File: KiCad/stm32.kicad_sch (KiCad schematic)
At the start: 20 parts, among them J15 Conn_01x04, J16 Conn_01x04, J17 Conn_01x04, J18 Conn_01x05, U7 STM32F030C8Tx, Y1 25MHz

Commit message: Add more footprints
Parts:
- C183, C184, C185, C186, C187, C188, C189, C190, C191, C192: footprint (none) -> Capacitor_SMD:C_0603_1608Metric
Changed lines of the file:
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@@
 			)
 		)
-		(property "Footprint" ""
+		(property "Footprint" "Capacitor_SMD:C_0603_1608Metric"
 			(at 110.49 80.01 0)
 			(effects
@@
 			)
 		)
-		(property "Footprint" ""
+		(property "Footprint" "Capacitor_SMD:C_0603_1608Metric"
 			(at 132.08 77.47 0)
 			(effects
@@
 			)
 		)
-		(property "Footprint" ""
+		(property "Footprint" "Capacitor_SMD:C_0603_1608Metric"
 			(at 110.49 74.93 0)
 			(effects
@@
 			)
 		)
-		(property "Footprint" ""
+		(property "Footprint" "Capacitor_SMD:C_0603_1608Metric"
 			(at 132.08 80.01 0)
 			(effects
@@
 			)
 		)
-		(property "Footprint" ""
+		(property "Footprint" "Capacitor_SMD:C_0603_1608Metric"
 			(at 87.63 109.22 0)
 			(effects
@@
 			)
 		)
-		(property "Footprint" ""
+		(property "Footprint" "Capacitor_SMD:C_0603_1608Metric"
 			(at 110.49 77.47 0)
 			(effects
@@
 			)
 		)
-		(property "Footprint" ""
+		(property "Footprint" "Capacitor_SMD:C_0603_1608Metric"
 			(at 151.13 93.98 0)
 			(effects
@@
 			)
 		)
-		(property "Footprint" ""
+		(property "Footprint" "Capacitor_SMD:C_0603_1608Metric"
 			(at 110.49 72.39 0)
 			(effects
@@
 			)
 		)
-		(property "Footprint" ""
+		(property "Footprint" "Capacitor_SMD:C_0603_1608Metric"
 			(at 151.13 100.33 0)
 			(effects
@@
 			)
 		)
-		(property "Footprint" ""
+		(property "Footprint" "Capacitor_SMD:C_0603_1608Metric"
 			(at 87.63 99.06 0)
 			(effects

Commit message: Add most passive component footprints
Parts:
- C183, C184, C185, C186, C187, C188, C189, C190, C191, C192: footprint Capacitor_SMD:C_0603_1608Metric -> Capacitor_SMD:C_0402_1005Metric
- R114, R115, R116: footprint (none) -> Resistor_SMD:R_0402_1005Metric
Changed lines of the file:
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@@
 			)
 		)
-		(property "Footprint" "Capacitor_SMD:C_0603_1608Metric"
+		(property "Footprint" "Capacitor_SMD:C_0402_1005Metric"
 			(at 110.49 80.01 0)
 			(effects
@@
 			)
 		)
-		(property "Footprint" "Capacitor_SMD:C_0603_1608Metric"
+		(property "Footprint" "Capacitor_SMD:C_0402_1005Metric"
 			(at 132.08 77.47 0)
 			(effects
@@
 			)
 		)
-		(property "Footprint" "Capacitor_SMD:C_0603_1608Metric"
+		(property "Footprint" "Capacitor_SMD:C_0402_1005Metric"
 			(at 110.49 74.93 0)
 			(effects
@@
 			)
 		)
-		(property "Footprint" ""
+		(property "Footprint" "Resistor_SMD:R_0402_1005Metric"
 			(at 101.6 93.98 0)
 			(effects
@@
 			)
 		)
-		(property "Footprint" "Capacitor_SMD:C_0603_1608Metric"
+		(property "Footprint" "Capacitor_SMD:C_0402_1005Metric"
 			(at 132.08 80.01 0)
 			(effects
@@
 			)
 		)
-		(property "Footprint" "Capacitor_SMD:C_0603_1608Metric"
+		(property "Footprint" "Capacitor_SMD:C_0402_1005Metric"
 			(at 87.63 109.22 0)
 			(effects
@@
 			)
 		)
-		(property "Footprint" "Capacitor_SMD:C_0603_1608Metric"
+		(property "Footprint" "Capacitor_SMD:C_0402_1005Metric"
 			(at 110.49 77.47 0)
 			(effects
@@
 			)
 		)
-		(property "Footprint" "Capacitor_SMD:C_0603_1608Metric"
+		(property "Footprint" "Capacitor_SMD:C_0402_1005Metric"
 			(at 151.13 93.98 0)
 			(effects
@@
 			)
 		)
-		(property "Footprint" "Capacitor_SMD:C_0603_1608Metric"
+		(property "Footprint" "Capacitor_SMD:C_0402_1005Metric"
 			(at 110.49 72.39 0)
 			(effects
@@
 			)
 		)
-		(property "Footprint" "Capacitor_SMD:C_0603_1608Metric"
+		(property "Footprint" "Capacitor_SMD:C_0402_1005Metric"
 			(at 151.13 100.33 0)
 			(effects
@@
 			)
 		)
-		(property "Footprint" ""
+		(property "Footprint" "Resistor_SMD:R_0402_1005Metric"
 			(at 179.07 82.55 0)
 			(effects
@@
 			)
 		)
-		(property "Footprint" ""
+		(property "Footprint" "Resistor_SMD:R_0402_1005Metric"
 			(at 181.61 82.55 0)
 			(effects
@@
 			)
 		)
-		(property "Footprint" "Capacitor_SMD:C_0603_1608Metric"
+		(property "Footprint" "Capacitor_SMD:C_0402_1005Metric"
 			(at 87.63 99.06 0)
 			(effects

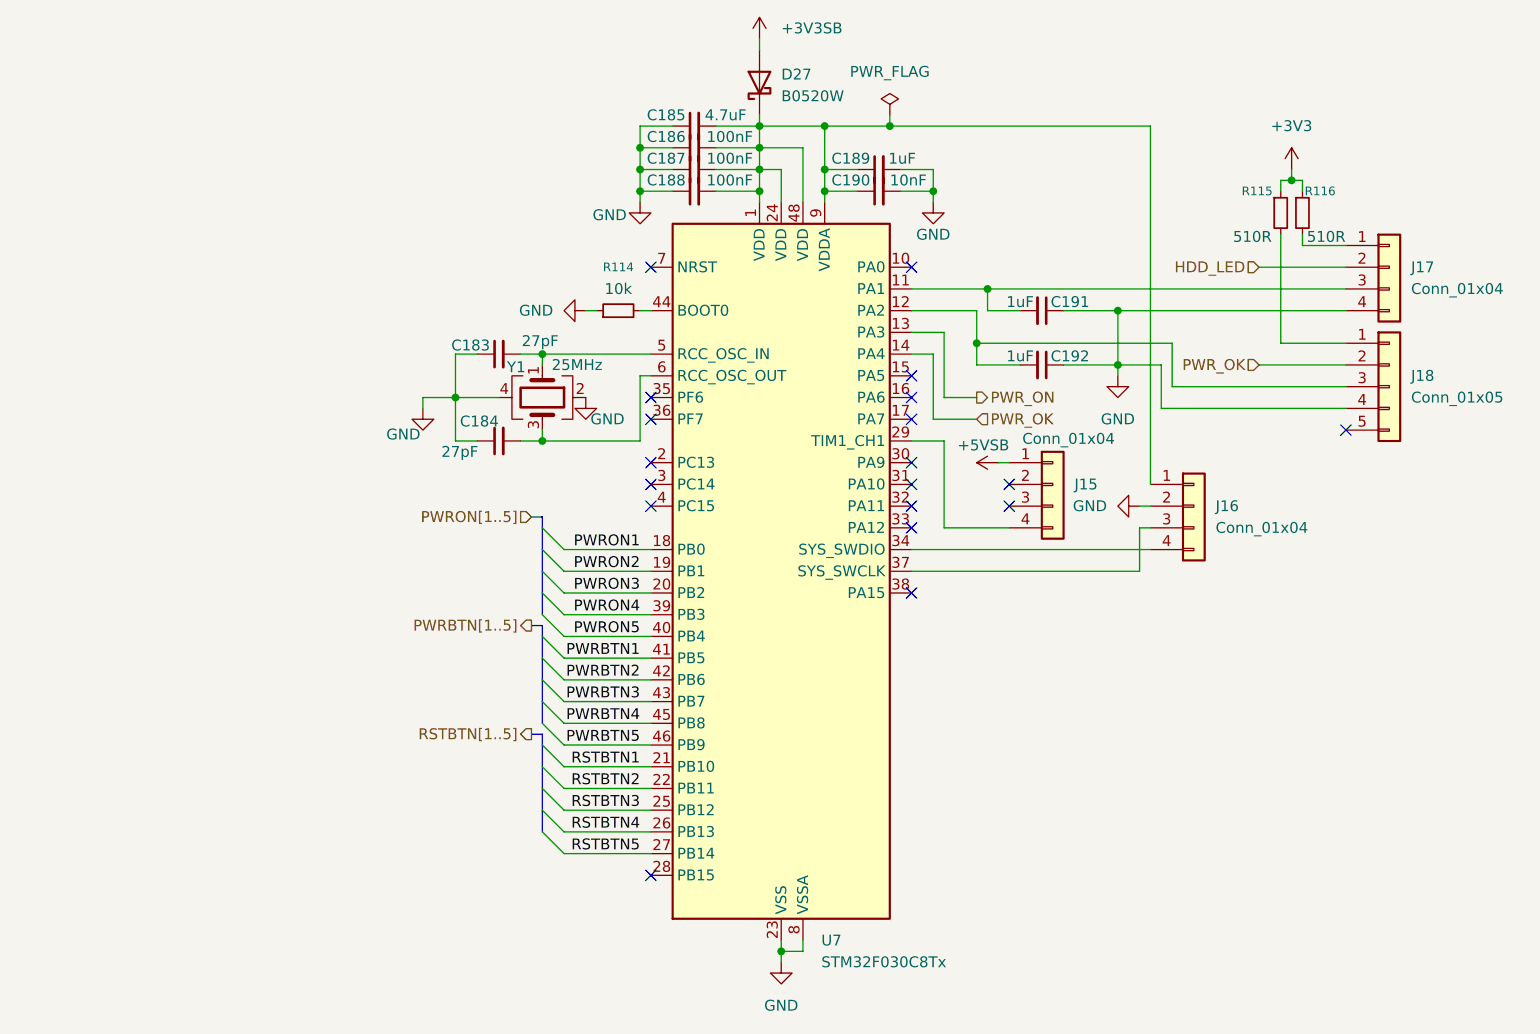
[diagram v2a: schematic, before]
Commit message: Finish fixing footprints
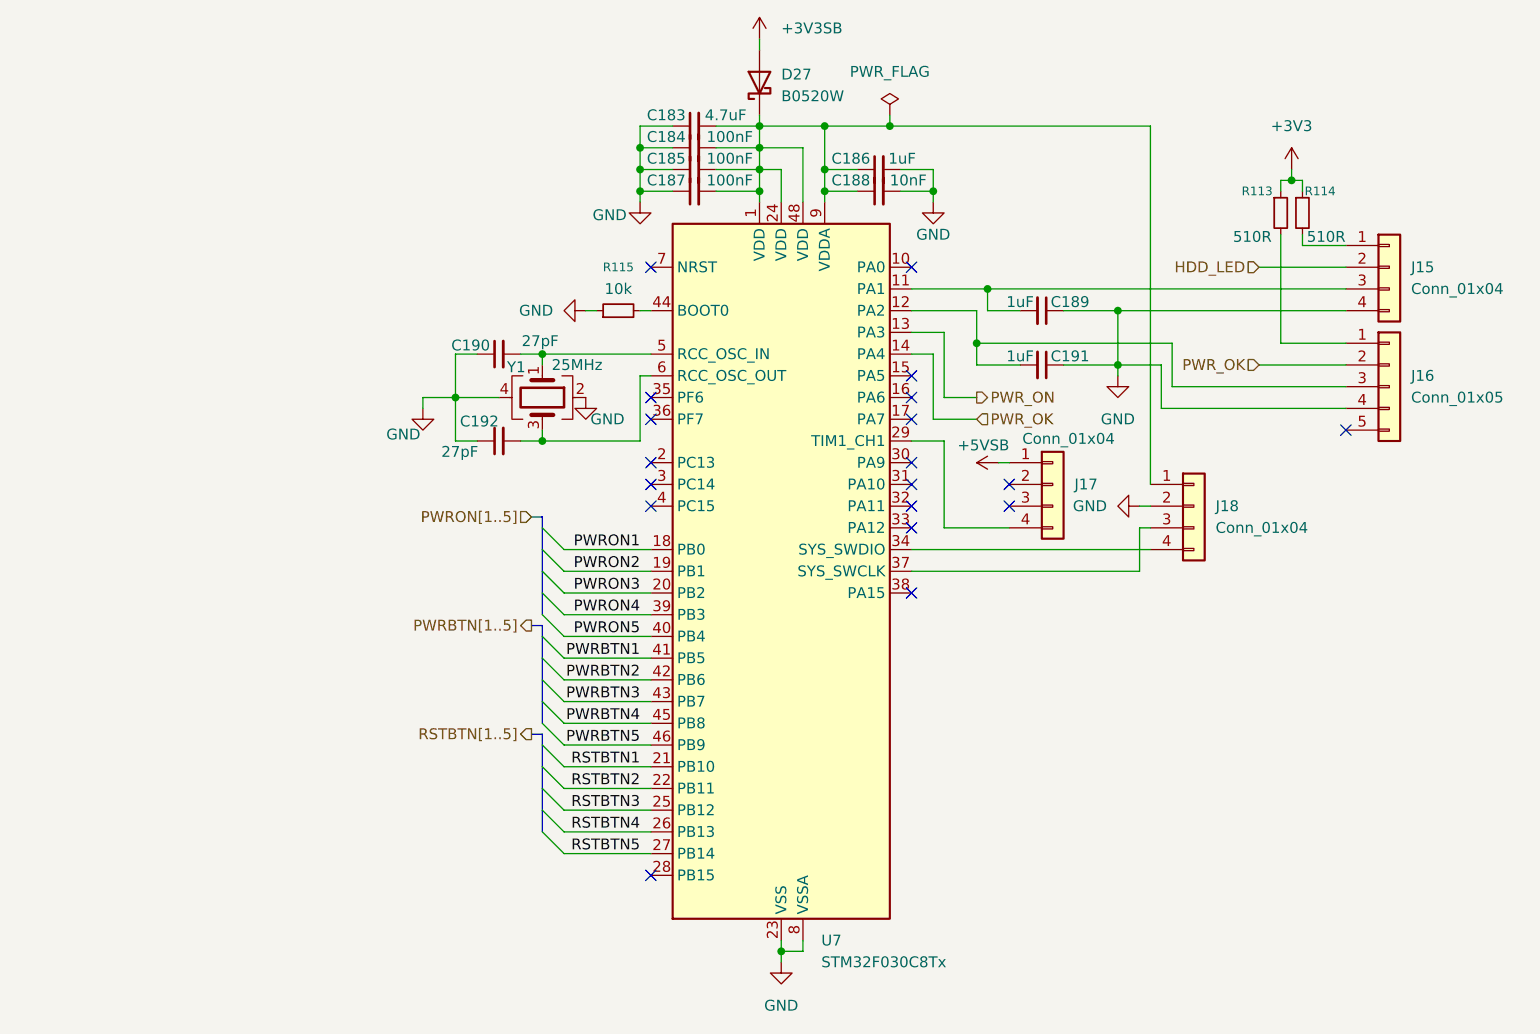
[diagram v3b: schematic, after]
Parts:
- renumbered C185 to C183, C186 to C184, C187 to C185, C189 to C186, C188 to C187, C190 to C188, C191 to C189, C183 to C190, C192 to C191, C184 to C192, J17 to J15, J18 to J16, J15 to J17, J16 to J18, R115 to R113, R116 to R114, R114 to R115
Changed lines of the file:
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@@
 		(dnp no)
 		(fields_autoplaced yes)
-		(property "Reference" "J17"
+		(property "Reference" "J15"
 			(at 194.31 88.8999 0)
 			(effects
@@
 			(project ""
 				(path "/49abeb3a-c598-45a3-ba6b-595eb04f17a8/6eac886f-f669-4a66-b218-dbac55577930"
-					(reference "J17")
+					(reference "J15")
 					(unit 1)
 				)
@@
 		(on_board yes)
 		(dnp no)
-		(property "Reference" "C188"
+		(property "Reference" "C187"
 			(at 109.474 78.74 90)
 			(effects
@@
 			(project ""
 				(path "/49abeb3a-c598-45a3-ba6b-595eb04f17a8/6eac886f-f669-4a66-b218-dbac55577930"
-					(reference "C188")
+					(reference "C187")
 					(unit 1)
 				)
@@
 		(on_board yes)
 		(dnp no)
-		(property "Reference" "C189"
+		(property "Reference" "C186"
 			(at 131.064 76.2 90)
 			(effects
@@
 			(project "LattePandaMuCluster"
 				(path "/49abeb3a-c598-45a3-ba6b-595eb04f17a8/6eac886f-f669-4a66-b218-dbac55577930"
-					(reference "C189")
+					(reference "C186")
 					(unit 1)
 				)
@@
 		(on_board yes)
 		(dnp no)
-		(property "Reference" "C186"
+		(property "Reference" "C184"
 			(at 109.474 73.66 90)
 			(effects
@@
 			(project "LattePandaMuCluster"
 				(path "/49abeb3a-c598-45a3-ba6b-595eb04f17a8/6eac886f-f669-4a66-b218-dbac55577930"
-					(reference "C186")
+					(reference "C184")
 					(unit 1)
 				)
@@
 		(on_board yes)
 		(dnp no)
-		(property "Reference" "#PWR0159"
+		(property "Reference" "#PWR0177"
 			(at 78.74 111.76 0)
 			(effects
@@
 			(project "LattePandaMuCluster"
 				(path "/49abeb3a-c598-45a3-ba6b-595eb04f17a8/6eac886f-f669-4a66-b218-dbac55577930"
-					(reference "#PWR0159")
+					(reference "#PWR0177")
 					(unit 1)
 				)
@@
 		(on_board yes)
 		(dnp no)
-		(property "Reference" "J16"
+		(property "Reference" "J18"
 			(at 171.45 116.8399 0)
 			(effects
@@
 			(project ""
 				(path "/49abeb3a-c598-45a3-ba6b-595eb04f17a8/6eac886f-f669-4a66-b218-dbac55577930"
-					(reference "J16")
+					(reference "J18")
 					(unit 1)
 				)
@@
 		(dnp no)
 		(fields_autoplaced yes)
-		(property "Reference" "R114"
+		(property "Reference" "R115"
 			(at 101.6 88.9 90)
 			(effects
@@
 			(project ""
 				(path "/49abeb3a-c598-45a3-ba6b-595eb04f17a8/6eac886f-f669-4a66-b218-dbac55577930"
-					(reference "R114")
+					(reference "R115")
 					(unit 1)
 				)
@@
 		(on_board yes)
 		(dnp no)
-		(property "Reference" "#PWR0161"
+		(property "Reference" "#PWR0176"
 			(at 97.79 110.49 0)
 			(effects
@@
 			(project "LattePandaMuCluster"
 				(path "/49abeb3a-c598-45a3-ba6b-595eb04f17a8/6eac886f-f669-4a66-b218-dbac55577930"
-					(reference "#PWR0161")
+					(reference "#PWR0176")
 					(unit 1)
 				)
@@
 		(on_board yes)
 		(dnp no)
-		(property "Reference" "C190"
+		(property "Reference" "C188"
 			(at 131.064 78.74 90)
 			(effects
@@
 			(project "LattePandaMuCluster"
 				(path "/49abeb3a-c598-45a3-ba6b-595eb04f17a8/6eac886f-f669-4a66-b218-dbac55577930"
-					(reference "C190")
+					(reference "C188")
 					(unit 1)
 				)
@@
 		(on_board yes)
 		(dnp no)
-		(property "Reference" "C184"
+		(property "Reference" "C192"
 			(at 85.344 106.934 90)
 			(effects
@@
 			(project "LattePandaMuCluster"
 				(path "/49abeb3a-c598-45a3-ba6b-595eb04f17a8/6eac886f-f669-4a66-b218-dbac55577930"
-					(reference "C184")
+					(reference "C192")
 					(unit 1)
 				)
@@
 		(dnp no)
 		(fields_autoplaced yes)
-		(property "Reference" "#PWR0167"
+		(property "Reference" "#PWR0175"
 			(at 160.02 107.95 0)
 			(effects
@@
 			(project ""
 				(path "/49abeb3a-c598-45a3-ba6b-595eb04f17a8/6eac886f-f669-4a66-b218-dbac55577930"
-					(reference "#PWR0167")
+					(reference "#PWR0175")
 					(unit 1)
 				)
@@
 		(on_board yes)
 		(dnp no)
-		(property "Reference" "#PWR0166"
+		(property "Reference" "#PWR0178"
 			(at 149.86 111.76 0)
 			(effects
@@
 			(project ""
 				(path "/49abeb3a-c598-45a3-ba6b-595eb04f17a8/6eac886f-f669-4a66-b218-dbac55577930"
-					(reference "#PWR0166")
+					(reference "#PWR0178")
 					(unit 1)
 				)
@@
 		(on_board yes)
 		(dnp no)
-		(property "Reference" "C187"
+		(property "Reference" "C185"
 			(at 109.474 76.2 90)
 			(effects
@@
 			(project "LattePandaMuCluster"
 				(path "/49abeb3a-c598-45a3-ba6b-595eb04f17a8/6eac886f-f669-4a66-b218-dbac55577930"
-					(reference "C187")
+					(reference "C185")
 					(unit 1)
 				)
@@
 		(on_board yes)
 		(dnp no)
-		(property "Reference" "C191"
+		(property "Reference" "C189"
 			(at 154.432 92.964 90)
 			(effects
@@
 			(project ""
 				(path "/49abeb3a-c598-45a3-ba6b-595eb04f17a8/6eac886f-f669-4a66-b218-dbac55577930"
-					(reference "C191")
+					(reference "C189")
 					(unit 1)
 				)
@@
 		(dnp no)
 		(fields_autoplaced yes)
-		(property "Reference" "#PWR0169"
+		(property "Reference" "#PWR0171"
 			(at 180.34 81.28 0)
 			(effects
@@
 			(project ""
 				(path "/49abeb3a-c598-45a3-ba6b-595eb04f17a8/6eac886f-f669-4a66-b218-dbac55577930"
-					(reference "#PWR0169")
+					(reference "#PWR0171")
 					(unit 1)
 				)
@@
 		(dnp no)
 		(fields_autoplaced yes)
-		(property "Reference" "#PWR0164"
+		(property "Reference" "#PWR0180"
 			(at 120.65 176.53 0)
 			(effects
@@
 			(project ""
 				(path "/49abeb3a-c598-45a3-ba6b-595eb04f17a8/6eac886f-f669-4a66-b218-dbac55577930"
-					(reference "#PWR0164")
+					(reference "#PWR0180")
 					(unit 1)
 				)
@@
 		(dnp no)
 		(fields_autoplaced yes)
-		(property "Reference" "#PWR0160"
+		(property "Reference" "#PWR0174"
 			(at 91.44 93.98 0)
 			(effects
@@
 			(project ""
 				(path "/49abeb3a-c598-45a3-ba6b-595eb04f17a8/6eac886f-f669-4a66-b218-dbac55577930"
-					(reference "#PWR0160")
+					(reference "#PWR0174")
 					(unit 1)
 				)
@@
 		(dnp no)
 		(fields_autoplaced yes)
-		(property "Reference" "J18"
+		(property "Reference" "J16"
 			(at 194.31 101.5999 0)
 			(effects
@@
 			(project ""
 				(path "/49abeb3a-c598-45a3-ba6b-595eb04f17a8/6eac886f-f669-4a66-b218-dbac55577930"
-					(reference "J18")
+					(reference "J16")
 					(unit 1)
 				)
@@
 		(on_board yes)
 		(dnp no)
-		(property "Reference" "C185"
+		(property "Reference" "C183"
 			(at 109.474 71.12 90)
 			(effects
@@
 			(project "LattePandaMuCluster"
 				(path "/49abeb3a-c598-45a3-ba6b-595eb04f17a8/6eac886f-f669-4a66-b218-dbac55577930"
-					(reference "C185")
+					(reference "C183")
 					(unit 1)
 				)
@@
 		(on_board yes)
 		(dnp no)
-		(property "Reference" "C192"
+		(property "Reference" "C191"
 			(at 154.432 99.314 90)
 			(effects
@@
 			(project "LattePandaMuCluster"
 				(path "/49abeb3a-c598-45a3-ba6b-595eb04f17a8/6eac886f-f669-4a66-b218-dbac55577930"
-					(reference "C192")
+					(reference "C191")
 					(unit 1)
 				)
@@
 		(on_board yes)
 		(dnp no)
-		(property "Reference" "R115"
+		(property "Reference" "R113"
 			(at 174.498 80.01 0)
 			(effects
@@
 			(project "LattePandaMuCluster"
 				(path "/49abeb3a-c598-45a3-ba6b-595eb04f17a8/6eac886f-f669-4a66-b218-dbac55577930"
-					(reference "R115")
+					(reference "R113")
 					(unit 1)
 				)
@@
 		(on_board yes)
 		(dnp no)
-		(property "Reference" "R116"
+		(property "Reference" "R114"
 			(at 181.864 80.01 0)
 			(effects
@@
 			(project ""
 				(path "/49abeb3a-c598-45a3-ba6b-595eb04f17a8/6eac886f-f669-4a66-b218-dbac55577930"
-					(reference "R116")
+					(reference "R114")
 					(unit 1)
 				)
@@
 		(on_board yes)
 		(dnp no)
-		(property "Reference" "#PWR0165"
+		(property "Reference" "#PWR0173"
 			(at 138.43 87.63 0)
 			(effects
@@
 			(project "LattePandaMuCluster"
 				(path "/49abeb3a-c598-45a3-ba6b-595eb04f17a8/6eac886f-f669-4a66-b218-dbac55577930"
-					(reference "#PWR0165")
+					(reference "#PWR0173")
 					(unit 1)
 				)
@@
 		(on_board yes)
 		(dnp no)
-		(property "Reference" "#PWR0162"
+		(property "Reference" "#PWR0172"
 			(at 104.14 87.63 0)
 			(effects
@@
 			(project ""
 				(path "/49abeb3a-c598-45a3-ba6b-595eb04f17a8/6eac886f-f669-4a66-b218-dbac55577930"
-					(reference "#PWR0162")
+					(reference "#PWR0172")
 					(unit 1)
 				)
@@
 		(dnp no)
 		(fields_autoplaced yes)
-		(property "Reference" "#PWR0168"
+		(property "Reference" "#PWR0179"
 			(at 156.21 116.84 0)
 			(effects
@@
 			(project ""
 				(path "/49abeb3a-c598-45a3-ba6b-595eb04f17a8/6eac886f-f669-4a66-b218-dbac55577930"
-					(reference "#PWR0168")
+					(reference "#PWR0179")
 					(unit 1)
 				)
@@
 		(on_board yes)
 		(dnp no)
-		(property "Reference" "C183"
+		(property "Reference" "C190"
 			(at 84.328 98.044 90)
 			(effects
@@
 			(project "LattePandaMuCluster"
 				(path "/49abeb3a-c598-45a3-ba6b-595eb04f17a8/6eac886f-f669-4a66-b218-dbac55577930"
-					(reference "C183")
+					(reference "C190")
 					(unit 1)
 				)
@@
 		(on_board yes)
 		(dnp no)
-		(property "Reference" "J15"
+		(property "Reference" "J17"
 			(at 154.94 114.2999 0)
 			(effects
@@
 			(project ""
 				(path "/49abeb3a-c598-45a3-ba6b-595eb04f17a8/6eac886f-f669-4a66-b218-dbac55577930"
-					(reference "J15")
+					(reference "J17")
 					(unit 1)
 				)
@@
 		(dnp no)
 		(fields_autoplaced yes)
-		(property "Reference" "#PWR0163"
+		(property "Reference" "#PWR0170"
 			(at 118.11 66.04 0)
 			(effects
@@
 			(project ""
 				(path "/49abeb3a-c598-45a3-ba6b-595eb04f17a8/6eac886f-f669-4a66-b218-dbac55577930"
-					(reference "#PWR0163")
-					(unit 1)
-				)
+					(reference "#PWR0170")
+					(unit 1)
+				)

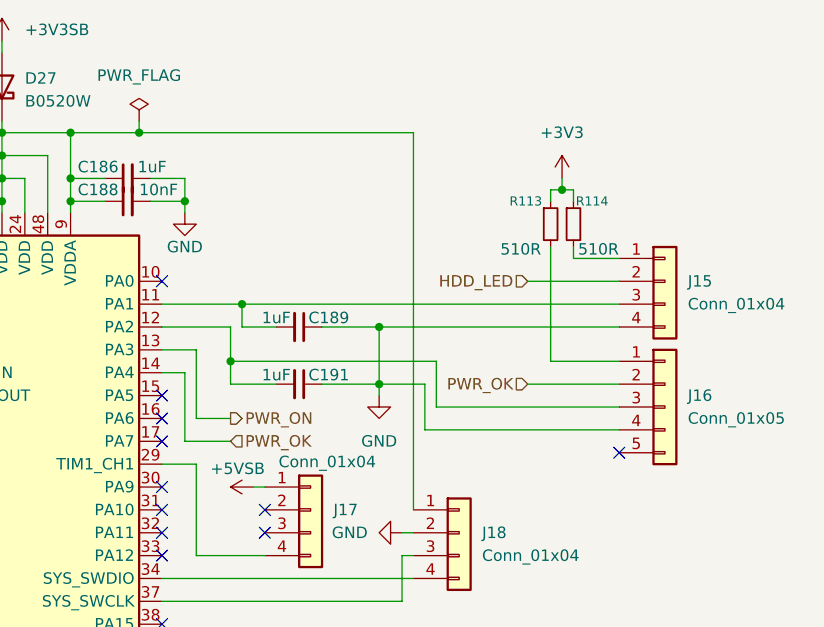
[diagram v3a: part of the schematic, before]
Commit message: Fix more footprint issues, continue laying out components
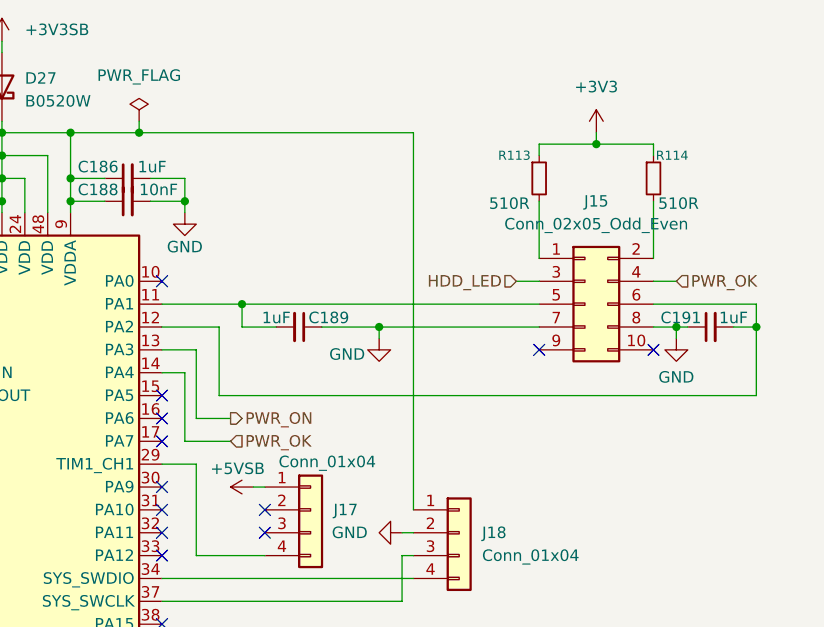
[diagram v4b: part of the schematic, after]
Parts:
- removed J15: Conn_01x04, Connector_PinHeader_2.54mm:PinHeader_1x04_P2.54mm_Vertical, symbol Connector_Generic:Conn_01x04
- removed J16: Conn_01x05, Connector_PinHeader_2.54mm:PinHeader_1x05_P2.54mm_Vertical, symbol Connector_Generic:Conn_01x05
- added J15: Conn_02x05_Odd_Even, Connector_PinHeader_2.54mm:PinHeader_2x05_P2.54mm_Vertical, symbol Connector_Generic:Conn_02x05_Odd_Even
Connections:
- net GND: now also J15.7 (Pin_7), J15.8 (Pin_8)
- net HDD_LED: now also J15.3 (Pin_3)
- net PWR_OK: now also J15.4 (Pin_4)
- net at R114.2: now also J15.2 (Pin_2)
- net at C189.2, U7.11 (PA1): now also J15.5 (Pin_5)
- net at R113.2: now also J15.1 (Pin_1)
- net at C191.2, U7.12 (PA2): now also J15.6 (Pin_6)
- no-connect marks 19 -> 20
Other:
- moved on the sheet: C191, R113, R114
